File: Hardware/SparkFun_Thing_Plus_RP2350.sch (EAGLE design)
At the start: 89 parts, among them J1 THING_PLUS_LOGICAL, J3 QWIIC_RIGHT_ANGLE, J6 MICRO-SD-ATOM, Q1 100mA/20V/3.8Ω, U1 RP2350A, U2 RM2, U3 RT9080-33GJ5, U4 LM66200, U5 W25QXX128MBIT, U6 MCP73831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

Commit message: Design review updates
Replace USB ESD diode with larger package for better manufacturing reliability
Add ordering instructions
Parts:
- removed D1: PRTR5V0U2F, SparkFun-IC-Power:PRTR5V0U2F
- added LOGO5: SPECIAL_INSTRUCTIONS-ORDERING, SparkFun-Aesthetics:SPECIAL_INSTRUCTIONS-ORDERING
- added U10: ESD Diode, SparkFun-DiscreteSemi:TVS_DIODE_ARRAY_DT1042-04SO-7
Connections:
- removed net N$24: D1.4, R10.1
- removed net N$25: D1.6, R11.1
- net GND: now also U10.VSS; no longer D1.2
- net N$7: now also R11.1, U10.IO1, U10.IO4; no longer D1.1
- net N$8: now also R10.1, U10.IO2, U10.IO3; no longer D1.3
- net V_USB: now also U10.VCC; no longer D1.5
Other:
- moved on the sheet: J4, R10, R11, R3, R4, SHLD

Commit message: Add PSRAM
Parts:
- added C26: 0.1uF, SparkFun-Capacitors:0.1UF-0402T-6.3V-10%-X7R
- added R23: 10k, SparkFun-Resistors:10KOHM-0402T-1/16W-1%
- added U11: APS6404L-3SQR-ZR, RP2350A:APS6404L-3SQR-ZR
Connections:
- new net PSRAM_!CS!: R23.1, U1.GPIO8, U11.!CE!
- net 3.3V: now also C26.1, R23.2, U11.VDD
- net GND: now also C26.2, U11.VSS
- net LED_IN: now also U1.GPIO14; no longer U1.GPIO8
- net QSPI_CLK: now also U11.SCLK
- net QSPI_D0: now also U11.SI/SIO0
- net QSPI_D1: now also U11.SO/SIO1
- net QSPI_D2: now also U11.SIO2
- net QSPI_D3: now also U11.SIO3
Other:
- note added: "8MB PSRAM"
- moved on the sheet: C12, C14, C15, C16, C17, C18, C19, C20, C21, C22, C7, C8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

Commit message: Bump version number to v10
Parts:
- FRAME1: REV v02 -> v10
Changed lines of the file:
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@@
 <part name="FRAME1" library="SparkFun-Aesthetics" deviceset="FRAME-LEDGER" device="">
 <attribute name="DESIGNER" value="Dryw Wade"/>
-<attribute name="REV" value="v02"/>
+<attribute name="REV" value="v10"/>
 </part>
 <part name="Y1" library="SparkFun-Clocks" deviceset="CRYSTAL-12MHZ" device="" value="12MHz"/>

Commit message: Design review updates
Rotate EN and BOOT flags to horizontal in schematic
Add warning about setting SPI pins high while uSD card is unpowered
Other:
- note added: "**WARNING** Do not set SPI pins high while the uSD card is unpowered. Doing so could damage the GPIO pins!"
- moved on the sheet: J6
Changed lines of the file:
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@@
 <text x="170.18" y="55.88" size="2.54" layer="94" font="vector" align="center">8MB PSRAM</text>
 <wire x1="111.76" y1="60.96" x2="228.6" y2="60.96" width="0.2032" layer="97" style="longdash"/>
+<text x="256.54" y="180.34" size="1.778" layer="97" font="vector" align="center">**WARNING**
+Do not set SPI pins high while the
+uSD card is unpowered. Doing so
+could damage the GPIO pins!</text>
 </plain>
 <instances>
@@
 <attribute name="VALUE" x="86.36" y="247.396" size="1.778" layer="96" font="vector" align="top-center"/>
 </instance>
-<instance part="GND43" gate="1" x="279.4" y="165.1" smashed="yes">
-<attribute name="VALUE" x="279.4" y="164.846" size="1.778" layer="96" font="vector" align="top-center"/>
+<instance part="GND43" gate="1" x="289.56" y="162.56" smashed="yes">
+<attribute name="VALUE" x="289.56" y="162.306" size="1.778" layer="96" font="vector" align="top-center"/>
 </instance>
 <instance part="SUPPLY41" gate="G$1" x="347.98" y="132.08" smashed="yes">
@@
 <attribute name="VALUE" x="177.8" y="241.046" size="1.778" layer="96" font="vector" align="top-center"/>
 </instance>
-<instance part="J6" gate="G$1" x="292.1" y="180.34" smashed="yes">
-<attribute name="NAME" x="284.48" y="196.088" size="1.778" layer="95" font="vector"/>
-<attribute name="VALUE" x="284.48" y="165.1" size="1.778" layer="96" font="vector"/>
+<instance part="J6" gate="G$1" x="302.26" y="177.8" smashed="yes">
+<attribute name="NAME" x="294.64" y="193.548" size="1.778" layer="95" font="vector"/>
+<attribute name="VALUE" x="294.64" y="162.56" size="1.778" layer="96" font="vector"/>
 </instance>
 <instance part="U9" gate="G$1" x="292.1" y="119.38" smashed="yes">
@@
 <attribute name="VALUE" x="40.64" y="38.354" size="1.778" layer="96" font="vector" align="bottom-center"/>
 </instance>
-<instance part="SUPPLY31" gate="G$1" x="279.4" y="195.58" smashed="yes">
-<attribute name="VALUE" x="279.4" y="198.374" size="1.778" layer="96" font="vector" align="bottom-center"/>
+<instance part="SUPPLY31" gate="G$1" x="289.56" y="193.04" smashed="yes">
+<attribute name="VALUE" x="289.56" y="195.834" size="1.778" layer="96" font="vector" align="bottom-center"/>
 </instance>
 <instance part="SUPPLY40" gate="G$1" x="391.16" y="195.58" smashed="yes">
@@
 <segment>
 <pinref part="GND43" gate="1" pin="GND"/>
-<wire x1="279.4" y1="167.64" x2="279.4" y2="170.18" width="0.1524" layer="91"/>
-<wire x1="279.4" y1="170.18" x2="281.94" y2="170.18" width="0.1524" layer="91"/>
+<wire x1="289.56" y1="165.1" x2="289.56" y2="167.64" width="0.1524" layer="91"/>
+<wire x1="289.56" y1="167.64" x2="292.1" y2="167.64" width="0.1524" layer="91"/>
 <pinref part="J6" gate="G$1" pin="VSS"/>
 <pinref part="J6" gate="G$1" pin="SHIELD"/>
-<wire x1="279.4" y1="170.18" x2="279.4" y2="172.72" width="0.1524" layer="91"/>
-<wire x1="279.4" y1="172.72" x2="281.94" y2="172.72" width="0.1524" layer="91"/>
-<junction x="279.4" y="170.18"/>
+<wire x1="289.56" y1="167.64" x2="289.56" y2="170.18" width="0.1524" layer="91"/>
+<wire x1="289.56" y1="170.18" x2="292.1" y2="170.18" width="0.1524" layer="91"/>
+<junction x="289.56" y="167.64"/>
 </segment>
 <segment>
@@
 </segment>
 <segment>
-<wire x1="281.94" y1="180.34" x2="279.4" y2="180.34" width="0.1524" layer="91"/>
-<label x="279.4" y="180.34" size="1.27" layer="95" font="vector" rot="R180" xref="yes"/>
+<wire x1="292.1" y1="177.8" x2="289.56" y2="177.8" width="0.1524" layer="91"/>
+<label x="289.56" y="177.8" size="1.27" layer="95" font="vector" rot="R180" xref="yes"/>
 <pinref part="J6" gate="G$1" pin="DAT0/SDO"/>
 </segment>
@@
 </segment>
 <segment>
-<wire x1="281.94" y1="175.26" x2="279.4" y2="175.26" width="0.1524" layer="91"/>
-<label x="279.4" y="175.26" size="1.27" layer="95" font="vector" rot="R180" xref="yes"/>
+<wire x1="292.1" y1="172.72" x2="289.56" y2="172.72" width="0.1524" layer="91"/>
+<label x="289.56" y="172.72" size="1.27" layer="95" font="vector" rot="R180" xref="yes"/>
 <pinref part="J6" gate="G$1" pin="CMD/SDI"/>
 </segment>
@@
 </segment>
 <segment>
-<wire x1="281.94" y1="177.8" x2="279.4" y2="177.8" width="0.1524" layer="91"/>
-<label x="279.4" y="177.8" size="1.27" layer="95" font="vector" rot="R180" xref="yes"/>
+<wire x1="292.1" y1="175.26" x2="289.56" y2="175.26" width="0.1524" layer="91"/>
+<label x="289.56" y="175.26" size="1.27" layer="95" font="vector" rot="R180" xref="yes"/>
 <pinref part="J6" gate="G$1" pin="CLK/SCK"/>
 </segment>
@@
 <wire x1="185.42" y1="228.6" x2="185.42" y2="236.22" width="0.1524" layer="91"/>
 <junction x="185.42" y="228.6"/>
-<label x="185.42" y="236.22" size="1.27" layer="95" font="vector" rot="R90" xref="yes"/>
+<label x="182.88" y="236.22" size="1.27" layer="95" font="vector" rot="R180" xref="yes"/>
+<wire x1="185.42" y1="236.22" x2="182.88" y2="236.22" width="0.1524" layer="91"/>
 </segment>
 </net>
@@
 <pinref part="R14" gate="G$1" pin="2"/>
 <wire x1="76.2" y1="190.5" x2="76.2" y2="193.04" width="0.1524" layer="91"/>
-<label x="76.2" y="193.04" size="1.27" layer="95" font="vector" rot="R90" xref="yes"/>
+<label x="73.66" y="193.04" size="1.27" layer="95" font="vector" rot="R180" xref="yes"/>
+<wire x1="76.2" y1="193.04" x2="73.66" y2="193.04" width="0.1524" layer="91"/>
 </segment>
 </net>
@@
 <net name="SD_!CS!" class="0">
 <segment>
-<wire x1="281.94" y1="187.96" x2="279.4" y2="187.96" width="0.1524" layer="91"/>
-<label x="279.4" y="187.96" size="1.27" layer="95" font="vector" rot="R180" xref="yes"/>
+<wire x1="292.1" y1="185.42" x2="289.56" y2="185.42" width="0.1524" layer="91"/>
+<label x="289.56" y="185.42" size="1.27" layer="95" font="vector" rot="R180" xref="yes"/>
 <pinref part="J6" gate="G$1" pin="DAT3/!CS!"/>
 </segment>
@@
 <segment>
 <pinref part="J6" gate="G$1" pin="DET"/>
-<wire x1="281.94" y1="190.5" x2="279.4" y2="190.5" width="0.1524" layer="91"/>
-<label x="279.4" y="190.5" size="1.27" layer="95" font="vector" rot="R180" xref="yes"/>
+<wire x1="292.1" y1="187.96" x2="289.56" y2="187.96" width="0.1524" layer="91"/>
+<label x="289.56" y="187.96" size="1.27" layer="95" font="vector" rot="R180" xref="yes"/>
 </segment>
 <segment>
@@
 </segment>
 <segment>
-<wire x1="281.94" y1="193.04" x2="279.4" y2="193.04" width="0.1524" layer="91"/>
-<wire x1="279.4" y1="193.04" x2="279.4" y2="195.58" width="0.1524" layer="91"/>
+<wire x1="292.1" y1="190.5" x2="289.56" y2="190.5" width="0.1524" layer="91"/>
+<wire x1="289.56" y1="190.5" x2="289.56" y2="193.04" width="0.1524" layer="91"/>
 <pinref part="J6" gate="G$1" pin="VDD"/>
 <pinref part="SUPPLY31" gate="G$1" pin="3.3V_SW"/>

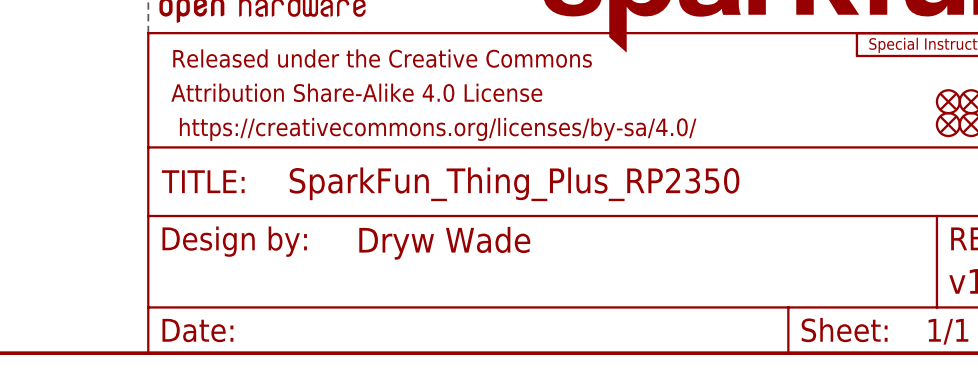
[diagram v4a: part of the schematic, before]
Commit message: Checklist review updates
Add "Based on design by:"
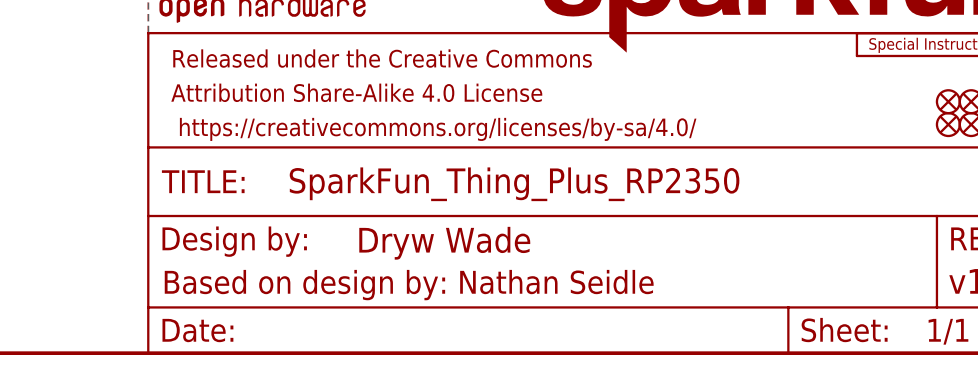
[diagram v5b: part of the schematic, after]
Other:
- note added: "Based on design by: Nathan Seidle"
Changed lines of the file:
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@@
 uSD card is unpowered. Doing so
 could damage the GPIO pins!</text>
+<text x="331.724" y="6.604" size="2.54" layer="94" font="vector">Based on design by: Nathan Seidle</text>
 </plain>
 <instances>
